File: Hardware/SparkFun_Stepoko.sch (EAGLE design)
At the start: 178 parts, among them J1 AVR ISP, Q1 16MHZ, Q2 100A/100V, U1 ATMEGA328, U2 CY7C65213, U3 74LVC1G04, U4 LM25011, U5 DRV8811, U6 74HC7014D, U7 74AHC1G08, U8 DRV8811, U9 DRV8811

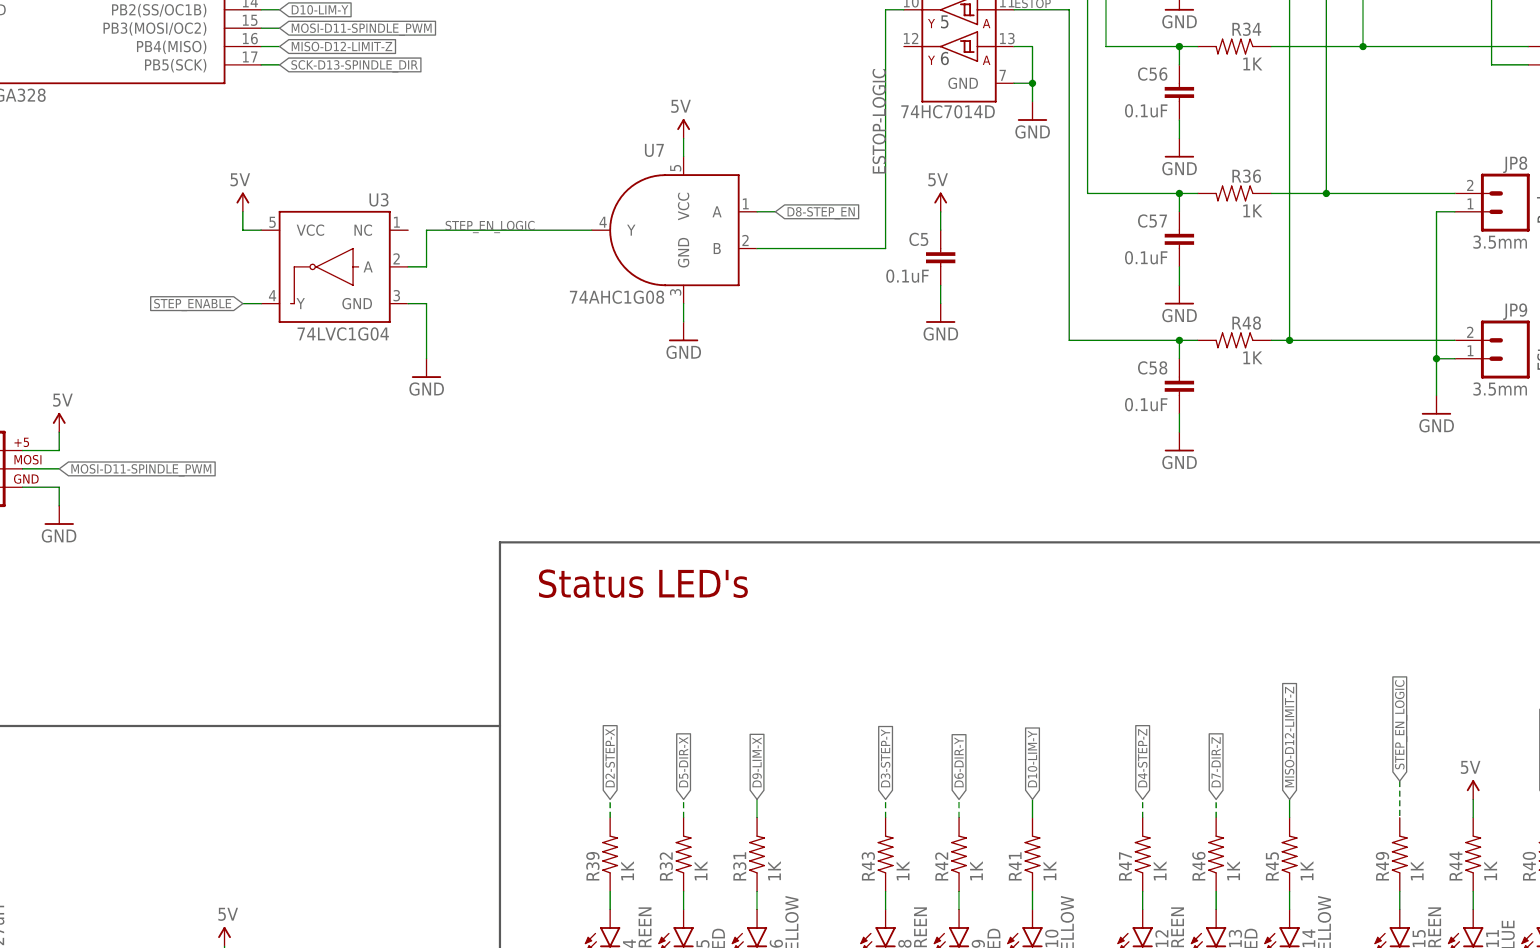
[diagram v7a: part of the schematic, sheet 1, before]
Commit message: fixing high impedance issues
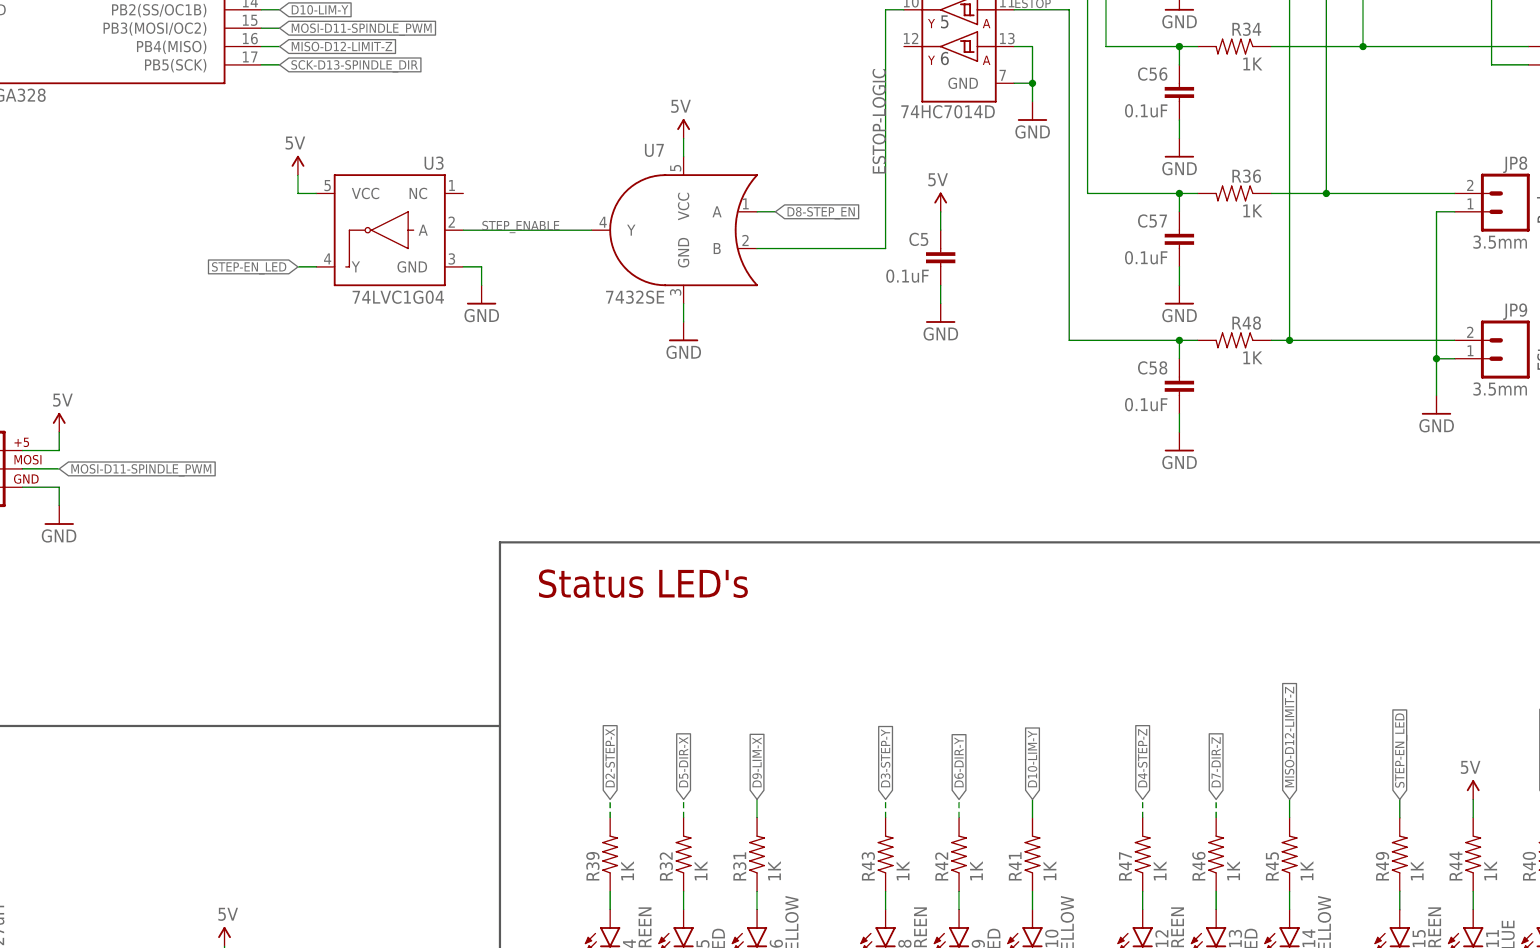
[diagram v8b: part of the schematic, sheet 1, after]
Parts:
- U7: value 74AHC1G08 -> 7432SE; device SparkFun-DigitalIC:74AHC1G08 -> SparkFun-DigitalIC:7432SE
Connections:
- removed net STEP_EN_LOGIC: R49.2, U3.A, U7.Y
- new net STEP-EN_LED: R49.2, U3.Y
- net STEP_ENABLE: now also U3.A, U7.Y; no longer U3.Y
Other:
- moved on the sheet: U3
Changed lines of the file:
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@@
 <layer number="91" name="Nets" color="2" fill="1" visible="yes" active="yes"/>
 <layer number="92" name="Busses" color="1" fill="1" visible="yes" active="yes"/>
-<layer number="93" name="Pins" color="2" fill="1" visible="yes" active="yes"/>
+<layer number="93" name="Pins" color="2" fill="1" visible="no" active="yes"/>
 <layer number="94" name="Symbols" color="4" fill="1" visible="yes" active="yes"/>
 <layer number="95" name="Names" color="7" fill="1" visible="yes" active="yes"/>
@@
 <part name="JP6" library="SparkFun-Connectors" deviceset="POWER_JACK" device="PTH_LOCK" value="POWER"/>
 <part name="VIN" library="SparkFun-Connectors" deviceset="M02" device="3.5MM_LOCK" value="3.5mm"/>
-<part name="U3" library="SparkFun-DigitalIC" deviceset="INVERTER" device="_SOT353-5" value="74LVC1G04"/>
-<part name="U7" library="SparkFun-DigitalIC" deviceset="74AHC1G08" device=""/>
+<part name="U7" library="SparkFun-DigitalIC" deviceset="74*32" device="SE"/>
 <part name="GND39" library="SparkFun" deviceset="GND" device=""/>
 <part name="C53" library="SparkFun-Capacitors" deviceset="0.1UF-25V(+80/-20%)(0603)" device="" value="0.1uF"/>
@@
 <part name="C3" library="SparkFun-Capacitors" deviceset="0.1UF-25V(+80/-20%)(0603)" device="" value="0.1uF"/>
 <part name="GND50" library="SparkFun" deviceset="GND" device=""/>
-<part name="GND51" library="SparkFun" deviceset="GND" device=""/>
-<part name="SUPPLY2" library="SparkFun-Aesthetics" deviceset="5V" device=""/>
 <part name="SUPPLY14" library="SparkFun-Aesthetics" deviceset="5V" device=""/>
 <part name="SUPPLY15" library="SparkFun-Aesthetics" deviceset="5V" device=""/>
@@
 <part name="D15" library="SparkFun-LED" deviceset="LED-GREEN" device="LILYPAD" value="GREEN"/>
 <part name="R49" library="SparkFun-Resistors" deviceset="1KOHM-1/10W-1%(0603)" device="" value="1K"/>
-<part name="GND23" library="SparkFun" deviceset="GND" device=""/>
 <part name="Q2" library="SparkFun-DiscreteSemi" deviceset="MOSFET-NCHANNEL" device="PSMN7R0" value="100A/100V"/>
 <part name="R50" library="SparkFun-Resistors" deviceset="1KOHM1/10W1%(0603)" device="" value="1K"/>
@@
 <part name="GND72" library="SparkFun" deviceset="GND" device=""/>
 <part name="SUPPLY19" library="SparkFun-Aesthetics" deviceset="5V" device=""/>
+<part name="U3" library="SparkFun-DigitalIC" deviceset="INVERTER" device="_SOT353-5" value="74LVC1G04"/>
+<part name="SUPPLY2" library="SparkFun-Aesthetics" deviceset="5V" device=""/>
+<part name="GND23" library="SparkFun" deviceset="GND" device=""/>
+<part name="GND51" library="SparkFun" deviceset="GND" device=""/>
 </parts>
 <sheets>
@@
 <instance part="JP6" gate="G$1" x="25.4" y="60.96"/>
 <instance part="VIN" gate="G$1" x="20.32" y="40.64"/>
-<instance part="U3" gate="G$1" x="251.46" y="160.02" rot="MR0"/>
 <instance part="U7" gate="G$1" x="299.72" y="165.1" rot="MR0"/>
 <instance part="GND39" gate="1" x="40.64" y="203.2"/>
@@
 <instance part="C3" gate="G$1" x="337.82" y="238.76" rot="MR0"/>
 <instance part="GND50" gate="1" x="337.82" y="231.14" rot="MR0"/>
-<instance part="GND51" gate="1" x="264.16" y="144.78" rot="MR0"/>
-<instance part="SUPPLY2" gate="G$1" x="238.76" y="167.64" rot="MR0"/>
 <instance part="SUPPLY14" gate="G$1" x="299.72" y="177.8" rot="MR0"/>
 <instance part="SUPPLY15" gate="G$1" x="347.98" y="226.06" rot="MR0"/>
@@
 <instance part="D15" gate="G$1" x="398.78" y="68.58"/>
 <instance part="R49" gate="G$1" x="398.78" y="78.74" rot="R90"/>
-<instance part="GND23" gate="1" x="398.78" y="58.42"/>
 <instance part="Q2" gate="G$1" x="53.34" y="40.64" rot="MR270"/>
 <instance part="R50" gate="G$1" x="53.34" y="55.88" rot="MR270"/>
@@
 <instance part="GND72" gate="1" x="383.54" y="58.42"/>
 <instance part="SUPPLY19" gate="G$1" x="408.94" y="86.36" rot="MR0"/>
+<instance part="U3" gate="G$1" x="259.08" y="165.1" rot="MR0"/>
+<instance part="SUPPLY2" gate="G$1" x="246.38" y="172.72" rot="MR0"/>
+<instance part="GND23" gate="1" x="271.78" y="154.94" rot="MR0"/>
+<instance part="GND51" gate="1" x="398.78" y="58.42"/>
 </instances>
 <busses>
@@
 </segment>
 <segment>
-<pinref part="U3" gate="G$1" pin="GND"/>
-<pinref part="GND51" gate="1" pin="GND"/>
-<wire x1="261.62" y1="154.94" x2="264.16" y2="154.94" width="0.1524" layer="91"/>
-<wire x1="264.16" y1="154.94" x2="264.16" y2="147.32" width="0.1524" layer="91"/>
-</segment>
-<segment>
 <pinref part="U7" gate="G$1" pin="GND"/>
 <pinref part="GND52" gate="1" pin="GND"/>
@@
 <pinref part="GND17" gate="1" pin="GND"/>
 <wire x1="363.22" y1="60.96" x2="363.22" y2="63.5" width="0.1524" layer="91"/>
-</segment>
-<segment>
-<pinref part="D15" gate="G$1" pin="C"/>
-<pinref part="GND23" gate="1" pin="GND"/>
-<wire x1="398.78" y1="60.96" x2="398.78" y2="63.5" width="0.1524" layer="91"/>
 </segment>
 <segment>
@@
 <wire x1="309.88" y1="60.96" x2="309.88" y2="63.5" width="0.1524" layer="91"/>
 </segment>
+<segment>
+<pinref part="U3" gate="G$1" pin="GND"/>
+<pinref part="GND23" gate="1" pin="GND"/>
+<wire x1="269.24" y1="160.02" x2="271.78" y2="160.02" width="0.1524" layer="91"/>
+<wire x1="271.78" y1="160.02" x2="271.78" y2="157.48" width="0.1524" layer="91"/>
+</segment>
+<segment>
+<pinref part="D15" gate="G$1" pin="C"/>
+<pinref part="GND51" gate="1" pin="GND"/>
+<wire x1="398.78" y1="60.96" x2="398.78" y2="63.5" width="0.1524" layer="91"/>
+</segment>
 </net>
 <net name="AREF" class="0">
@@
 </segment>
 <segment>
-<pinref part="U3" gate="G$1" pin="VCC"/>
-<wire x1="241.3" y1="165.1" x2="238.76" y2="165.1" width="0.1524" layer="91"/>
-<wire x1="238.76" y1="165.1" x2="238.76" y2="167.64" width="0.1524" layer="91"/>
-<pinref part="SUPPLY2" gate="G$1" pin="5V"/>
-</segment>
-<segment>
 <pinref part="U7" gate="G$1" pin="VCC"/>
 <wire x1="299.72" y1="175.26" x2="299.72" y2="177.8" width="0.1524" layer="91"/>
@@
 <pinref part="SUPPLY19" gate="G$1" pin="5V"/>
 <wire x1="408.94" y1="86.36" x2="408.94" y2="83.82" width="0.1524" layer="91"/>
+</segment>
+<segment>
+<pinref part="U3" gate="G$1" pin="VCC"/>
+<pinref part="SUPPLY2" gate="G$1" pin="5V"/>
+<wire x1="248.92" y1="170.18" x2="246.38" y2="170.18" width="0.1524" layer="91"/>
+<wire x1="246.38" y1="170.18" x2="246.38" y2="172.72" width="0.1524" layer="91"/>
 </segment>
 </net>
@@
 <net name="STEP_ENABLE" class="0">
 <segment>
-<label x="238.76" y="154.94" size="1.27" layer="97" font="vector" ratio="10" rot="R180" xref="yes"/>
-<wire x1="241.3" y1="154.94" x2="238.76" y2="154.94" width="0.1524" layer="91"/>
-<pinref part="U3" gate="G$1" pin="Y"/>
+<wire x1="287.02" y1="165.1" x2="269.24" y2="165.1" width="0.1524" layer="91"/>
+<pinref part="U7" gate="G$1" pin="Y"/>
+<pinref part="U3" gate="G$1" pin="A"/>
+<label x="271.78" y="165.1" size="1.27" layer="95"/>
 </segment>
 <segment>
@@
 </segment>
 </net>
-<net name="STEP_EN_LOGIC" class="0">
-<segment>
-<pinref part="U7" gate="G$1" pin="Y"/>
-<pinref part="U3" gate="G$1" pin="A"/>
-<wire x1="261.62" y1="160.02" x2="264.16" y2="160.02" width="0.1524" layer="91"/>
-<wire x1="264.16" y1="160.02" x2="264.16" y2="165.1" width="0.1524" layer="91"/>
-<wire x1="264.16" y1="165.1" x2="287.02" y2="165.1" width="0.1524" layer="91"/>
-<label x="266.7" y="165.1" size="1.27" layer="95"/>
-</segment>
-<segment>
-<wire x1="398.78" y1="88.9" x2="398.78" y2="83.82" width="0.1524" layer="91" style="longdash"/>
+<net name="STEP-EN_LED" class="0">
+<segment>
+<pinref part="U3" gate="G$1" pin="Y"/>
+<wire x1="248.92" y1="160.02" x2="246.38" y2="160.02" width="0.1524" layer="91"/>
+<label x="246.38" y="160.02" size="1.27" layer="95" rot="R180" xref="yes"/>
+</segment>
+<segment>
 <pinref part="R49" gate="G$1" pin="2"/>
-<label x="398.78" y="88.9" size="1.27" layer="95" rot="R90" xref="yes"/>
-</segment>
-</net>
+<wire x1="398.78" y1="83.82" x2="398.78" y2="86.36" width="0.1524" layer="91"/>
+<label x="398.78" y="86.36" size="1.27" layer="95" rot="R90" xref="yes"/>
+</segment>
+</net>
